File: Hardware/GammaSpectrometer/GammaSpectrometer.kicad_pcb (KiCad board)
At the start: 2 copper layers, 100 x 100 mm, 59 parts, among them J1 power supply, J2 Conn_01x07_Female, Q1 AOD2810, U1 MCP1416

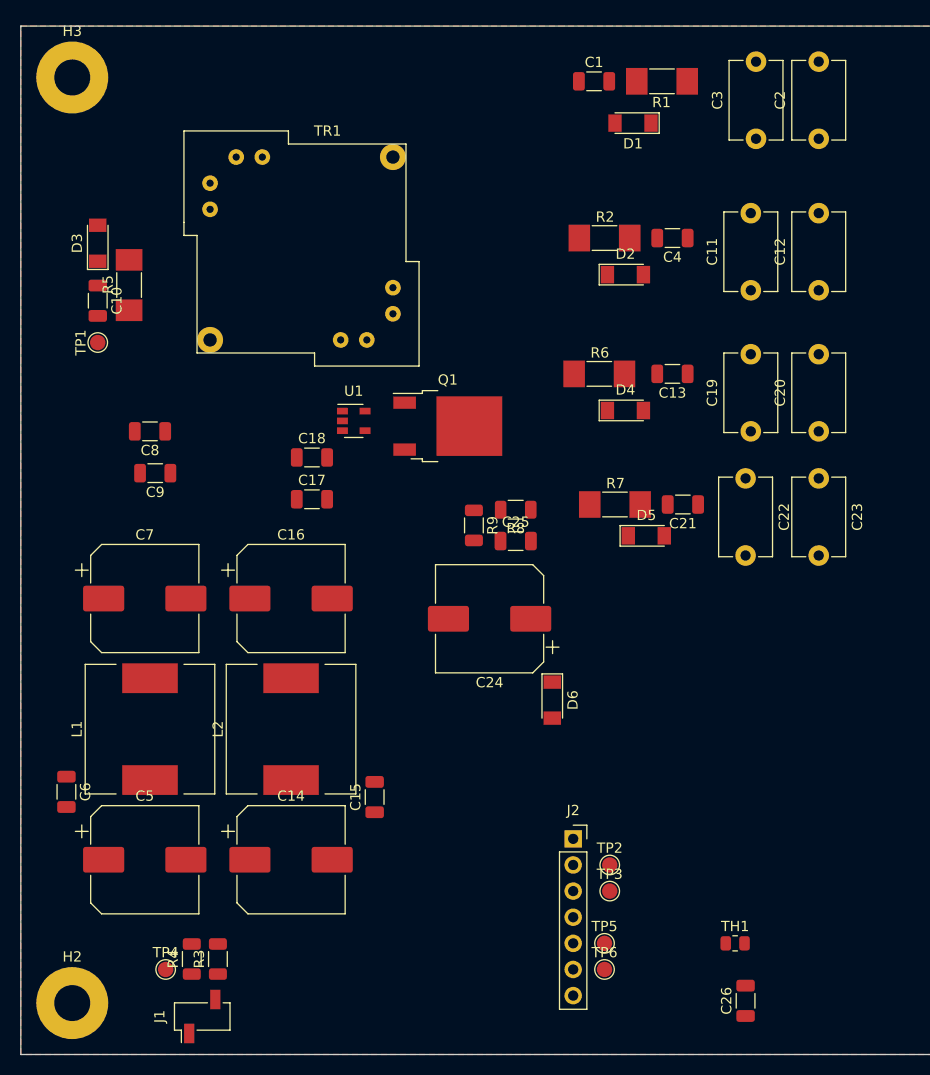
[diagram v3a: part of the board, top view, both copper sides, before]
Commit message: fixed footprints
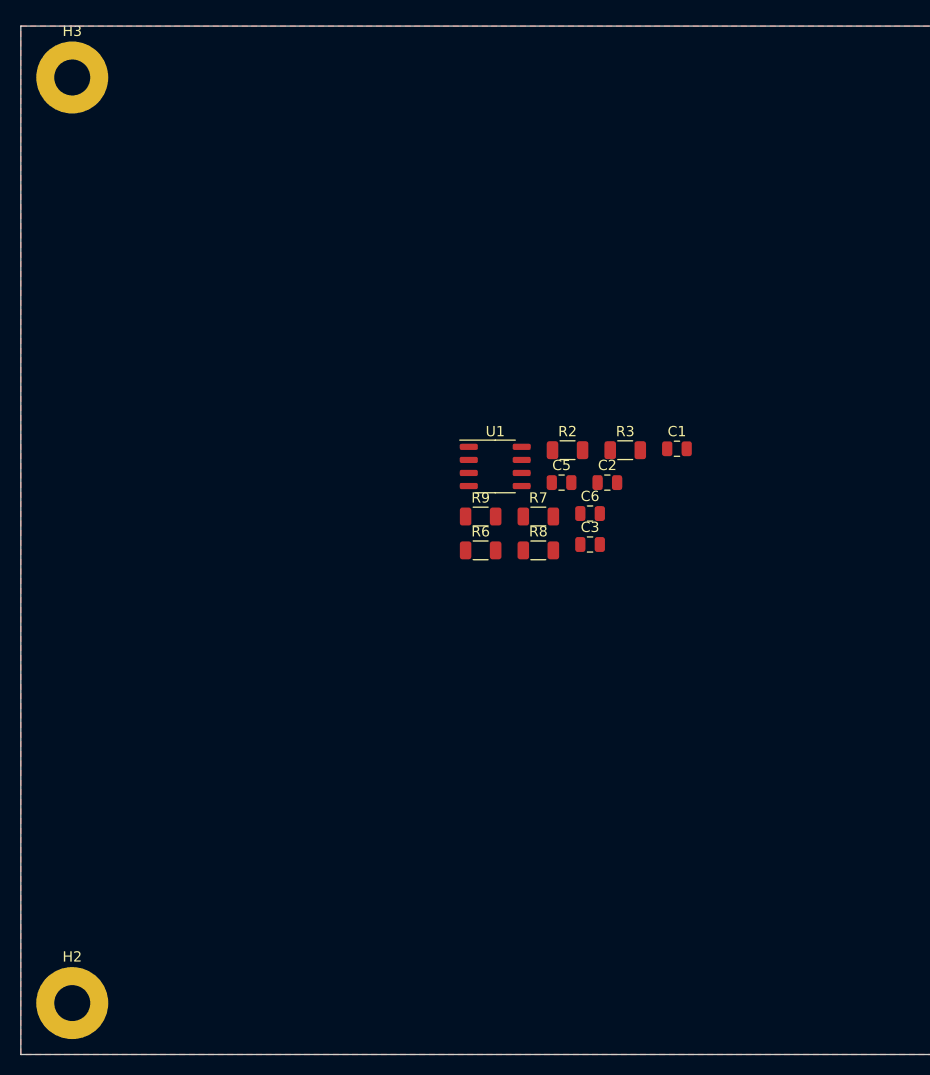
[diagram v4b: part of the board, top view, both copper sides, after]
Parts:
- removed C10, C13, C21, C4: TBD, Capacitor_SMD:C_1206_3216Metric
- removed C11, C12, C19, C20, C22, C23: 10n/2kV, Capacitor_THT:C_Disc_D7.5mm_W5.0mm_P7.50mm
- removed C14, C16, C7: 470u/25V, Capacitor_SMD:CP_Elec_10x10
- removed C15: 1u, Capacitor_SMD:C_1206_3216Metric
- removed C17, C18, C25: 100n, Capacitor_SMD:C_1206_3216Metric
- removed C24: 10u/12V, Capacitor_SMD:CP_Elec_10x10
- removed C26: 1n, Capacitor_SMD:C_1206_3216Metric
- removed C8, C9: 10u, Capacitor_SMD:C_1206_3216Metric
- removed D1, D2, D4, D5: HER208, Diode_SMD:D_MiniMELF
- removed D3: TBD, Diode_SMD:D_MiniMELF
- removed D6: D, Diode_SMD:D_MiniMELF
- removed J1: power supply, Connector_PinSocket_2.54mm:PinSocket_1x02_P2.54mm_Vertical_SMD_Pin1Left
- removed J2: Conn_01x07_Female, Connector_PinSocket_2.54mm:PinSocket_1x07_P2.54mm_Vertical
- removed L1: 560n, Inductor_SMD:L_12x12mm_H6mm
- removed L2: TBD, Inductor_SMD:L_12x12mm_H6mm
- removed Q1: AOD2810, Package_TO_SOT_SMD:TO-252-2
- removed R1, R5: TBD, Resistor_SMD:R_MELF_MMB-0207
- removed R4: 1R, Resistor_SMD:R_1206_3216Metric
- removed TH1: NTCS0805E3103FMT, Resistor_SMD:R_0805_2012Metric
- removed TP1: TestPoint, TestPoint:TestPoint_Pad_D1.5mm
- removed TP2: HV_MONITOR, TestPoint:TestPoint_Pad_D1.5mm
- removed TP3: ENABLE, TestPoint:TestPoint_Pad_D1.5mm
- removed TP4: IN_CURRENT_MONITOR_1, TestPoint:TestPoint_Pad_D1.5mm
- removed TP5: IN_CURRENT_MONITOR_2, TestPoint:TestPoint_Pad_D1.5mm
- removed TP6: TEMP_MONITOR, TestPoint:TestPoint_Pad_D1.5mm
- removed TR1: RM8, GammaSpectrometer:RM8
- C1: value TBD -> 220n; footprint Capacitor_SMD:C_1206_3216Metric -> Capacitor_SMD:C_0805_2012Metric
- C2: value 10n/2kV -> 220n; footprint Capacitor_THT:C_Disc_D7.5mm_W5.0mm_P7.50mm -> Capacitor_SMD:C_0805_2012Metric
- C3: value 10n/2kV -> C; footprint Capacitor_THT:C_Disc_D7.5mm_W5.0mm_P7.50mm -> Capacitor_SMD:C_0805_2012Metric
- C5: value 470u/25V -> C; footprint Capacitor_SMD:CP_Elec_10x10 -> Capacitor_SMD:C_0805_2012Metric
- C6: value 10u -> 470p; footprint Capacitor_SMD:C_1206_3216Metric -> Capacitor_SMD:C_0805_2012Metric
- R2: value TBD -> 1R; footprint Resistor_SMD:R_MELF_MMB-0207 -> Resistor_SMD:R_1206_3216Metric
- R6, R7: footprint Resistor_SMD:R_MELF_MMB-0207 -> Resistor_SMD:R_1206_3216Metric
- R8, R9: value 6k8 -> 1R
- U1: value MCP1416 -> UC2843; footprint Package_TO_SOT_SMD:SOT-23-5 -> Package_SO:SO-8_3.9x4.9mm_P1.27mm
- moved R3 63.4 mm to (208.8, 91.2), turned to 0 degrees
- moved C6 57.7 mm to (205.3, 97.4), turned to 0 degrees
- moved C5 54.7 mm to (202.6, 94.4)
- moved C3 42.6 mm to (205.3, 100.4), turned to 0 degrees
- moved C2 39.2 mm to (207.0, 94.4), turned to 0 degrees
- moved C1 36.6 mm to (213.8, 91.1)
- moved R2 20.9 mm to (203.2, 91.2)
- moved R6 20.7 mm to (194.7, 101.0)
- moved U1 14.5 mm to (196.1, 92.8)
- moved R7 7.54 mm to (200.3, 97.7)
- moved R8 4.52 mm to (200.3, 101.0), turned to 0 degrees
- moved R9 1.08 mm to (194.7, 97.7), turned to 0 degrees
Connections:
- net /HighVoltagePowerSupply/HV_MONITOR renamed Net-(R8-Pad2)
- C1 pad 1: Net-(C1-Pad1) -> /HighVoltagePowerSupply/GND_1
- C1 pad 2: Net-(C1-Pad2) -> VCC
- C2 pad 1: Net-(C11-Pad2) -> /HighVoltagePowerSupply/GND_1
- C2 pad 2: HV+ -> VCC
- C3 pad 1: Net-(C11-Pad2) -> Net-(C3-Pad1)
- C3 pad 2: HV+ -> Net-(C3-Pad2)
- C5 pad 1: /HighVoltagePowerSupply/IN_CURRENT_MONITOR_2 -> Net-(C5-Pad1)
- C6 pad 1: GND -> Net-(C6-Pad1)
- C6 pad 2: /HighVoltagePowerSupply/IN_CURRENT_MONITOR_2 -> unconnected-(C6-Pad2)
- R2 pad 1: Net-(C11-Pad2) -> Net-(D1-Pad1)
- R2 pad 2: Net-(C4-Pad2) -> Net-(R2-Pad2)
- R3 pad 1: /HighVoltagePowerSupply/IN_CURRENT_MONITOR_1 -> Net-(R2-Pad2)
- R3 pad 2: /HighVoltagePowerSupply/IN_CURRENT_MONITOR_2 -> Net-(C3-Pad1)
- R6 pad 1: Net-(C11-Pad1) -> Net-(Q1-Pad3)
- R6 pad 2: Net-(C13-Pad2) -> <NO NET>
- R7 pad 1: HV_REG+ -> Net-(Q1-Pad3)
- R7 pad 2: Net-(C21-Pad2) -> <NO NET>
- R8 pad 1: Net-(C24-Pad1) -> Net-(C3-Pad1)
- U1 pad 1: (no net) -> Net-(C3-Pad2)
- U1 pad 2: Net-(C16-Pad1) -> Net-(C3-Pad1)
- U1 pad 3: /HighVoltagePowerSupply/ENABLE -> Net-(C6-Pad1)
- U1 pad 4: GND -> Net-(C5-Pad1)
- U1 pad 5: Net-(Q1-Pad1) -> GND

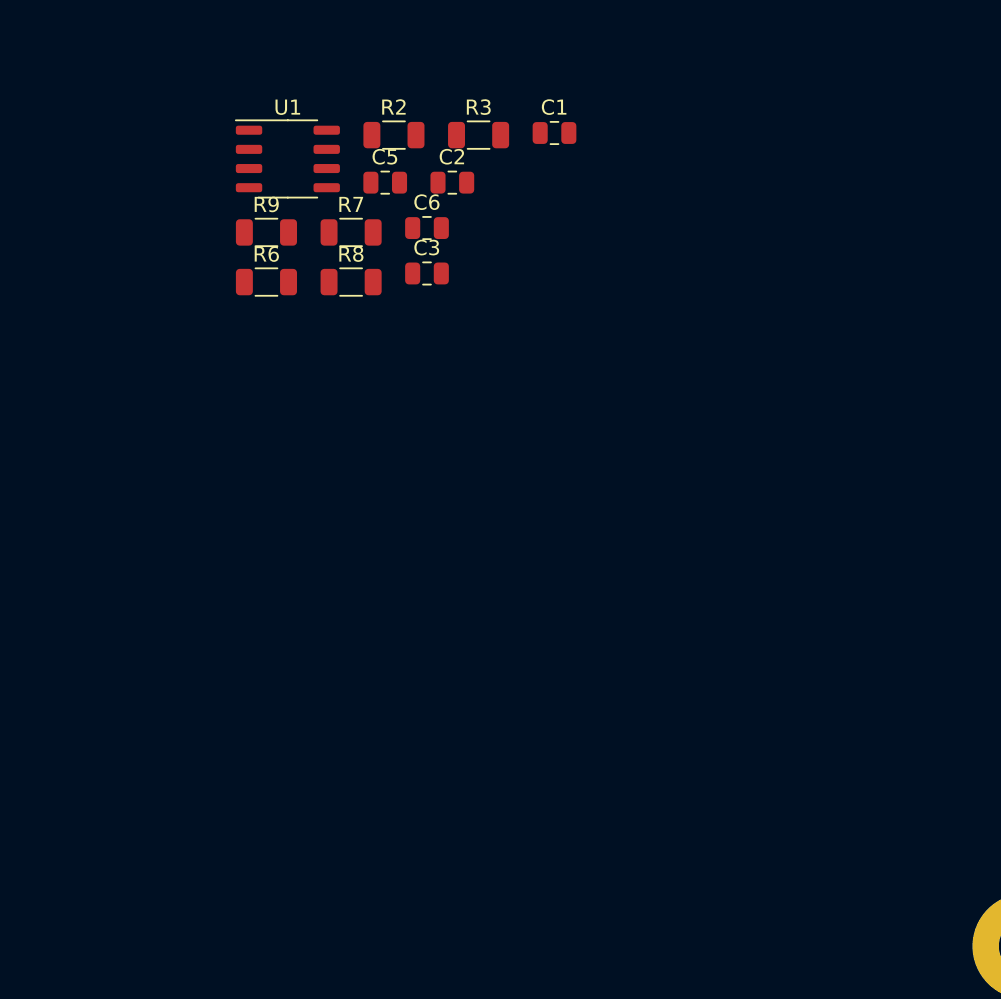
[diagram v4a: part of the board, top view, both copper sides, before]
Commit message: beggining draft of in-series hv power supply
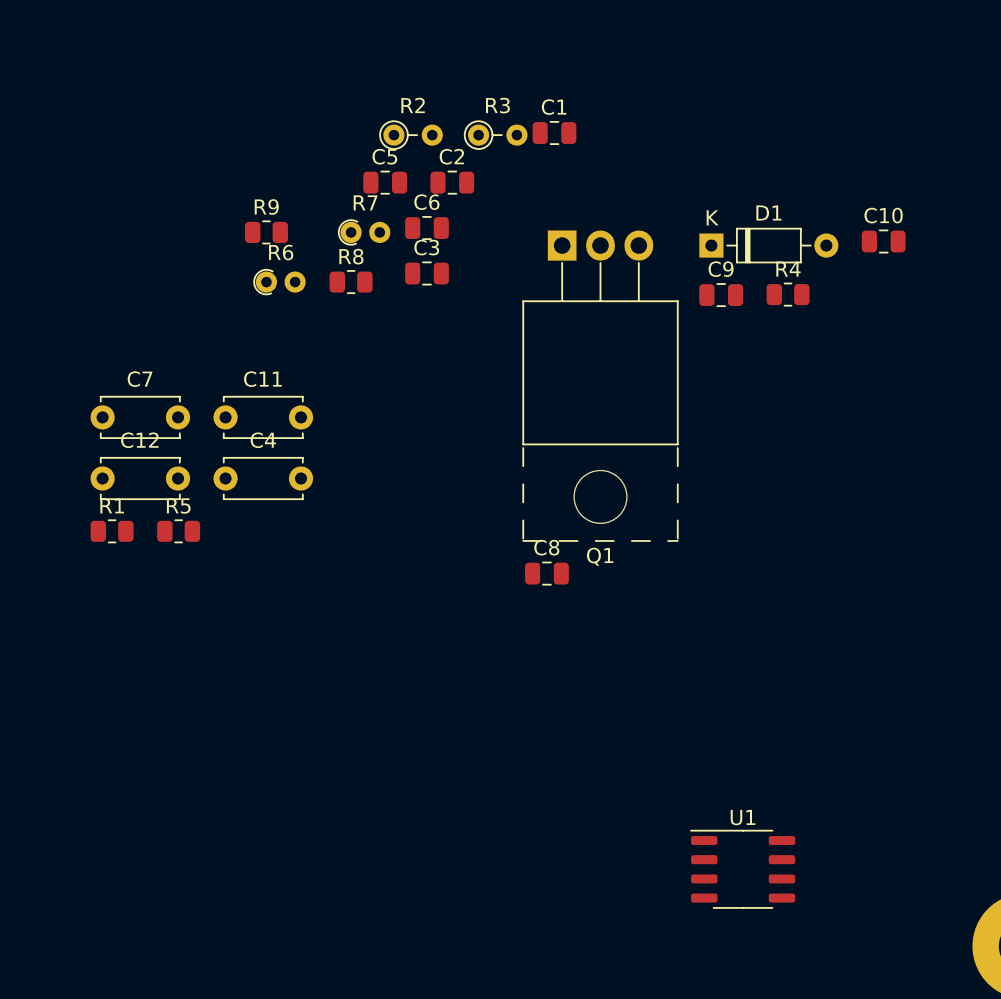
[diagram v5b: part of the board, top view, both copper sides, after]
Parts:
- added C10: TBD, Capacitor_SMD:C_0805_2012Metric, F.Cu at (235.6, 98.3)
- added C11: 100n/500V, Capacitor_THT:C_Disc_D5.0mm_W2.5mm_P5.00mm, F.Cu at (192.0, 110.0)
- added C12: 100n/500V, Capacitor_THT:C_Disc_D5.0mm_W2.5mm_P5.00mm, F.Cu at (183.8, 114.0)
- added C4: 100n/500V, Capacitor_THT:C_Disc_D5.0mm_W2.5mm_P5.00mm, F.Cu at (192.0, 114.0)
- added C7: 100n/500V, Capacitor_THT:C_Disc_D5.0mm_W2.5mm_P5.00mm, F.Cu at (183.8, 110.0)
- added C8: 100n, Capacitor_SMD:C_0805_2012Metric, F.Cu at (213.3, 120.3)
- added C9: 100n, Capacitor_SMD:C_0805_2012Metric, F.Cu at (224.8, 101.8)
- added D1: ER1K-DIO, Diode_THT:D_DO-35_SOD27_P7.62mm_Horizontal, F.Cu at (224.2, 98.6)
- added Q1: AOT1N60, Package_TO_SOT_THT:TO-220-3_Horizontal_TabUp, F.Cu at (214.3, 98.6)
- added R1: TBD, Resistor_SMD:R_0805_2012Metric, F.Cu at (184.5, 117.5)
- added R4: 10k, Resistor_SMD:R_0805_2012Metric, F.Cu at (229.3, 101.8)
- added R5: 1k, Resistor_SMD:R_0805_2012Metric, F.Cu at (188.9, 117.5)
- C1, C2: value 220n -> 100n
- C3, C5: value C -> TBD
- R2, R3: value 1R -> TBD; footprint Resistor_SMD:R_1206_3216Metric -> Resistor_THT:R_Axial_DIN0204_L3.6mm_D1.6mm_P2.54mm_Vertical
- R6, R7: footprint Resistor_SMD:R_1206_3216Metric -> Resistor_THT:R_Axial_DIN0204_L3.6mm_D1.6mm_P1.90mm_Vertical
- R8, R9: value 1R -> TBD; footprint Resistor_SMD:R_1206_3216Metric -> Resistor_SMD:R_0805_2012Metric
- moved U1 55.9 mm to (226.3, 139.9)
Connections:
- net VCC renamed +5V
- C1 pad 1: /HighVoltagePowerSupply/GND_1 -> DCDC1 V-
- C2 pad 1: /HighVoltagePowerSupply/GND_1 -> DCDC1 V-
- C3 pad 1: Net-(C3-Pad1) -> Net-(C6-Pad1)
- C5 pad 2: GND -> DCDC1 V-
- C6 pad 2: unconnected-(C6-Pad2) -> DCDC1 V-
- H1 pad 1: GND -> DCDC1 V-
- H2 pad 1: GND -> DCDC1 V-
- H3 pad 1: GND -> DCDC1 V-
- H4 pad 1: GND -> DCDC1 V-
- R2 pad 1: Net-(D1-Pad1) -> DCDC1 V+
- R3 pad 2: Net-(C3-Pad1) -> Net-(R3-Pad2)
- R6 pad 2: <NO NET> -> DCDC1 V-
- R7 pad 2: <NO NET> -> DCDC1 V-
- R8 pad 1: Net-(C3-Pad1) -> Net-(R3-Pad2)
- R9 pad 2: GND -> DCDC1 V-
- U1 pad 2: Net-(C3-Pad1) -> Net-(C6-Pad1)
- U1 pad 3: Net-(C6-Pad1) -> Net-(R3-Pad2)
- U1 pad 5: GND -> DCDC1 V-
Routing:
- added copper zone on F.Cu, net (none)
- removed copper zone on F.Cu, net GND
